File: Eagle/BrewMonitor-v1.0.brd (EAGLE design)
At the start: 41.6 x 50.2 mm, 18 parts, among them U1 ATMEGA328P_PDIP

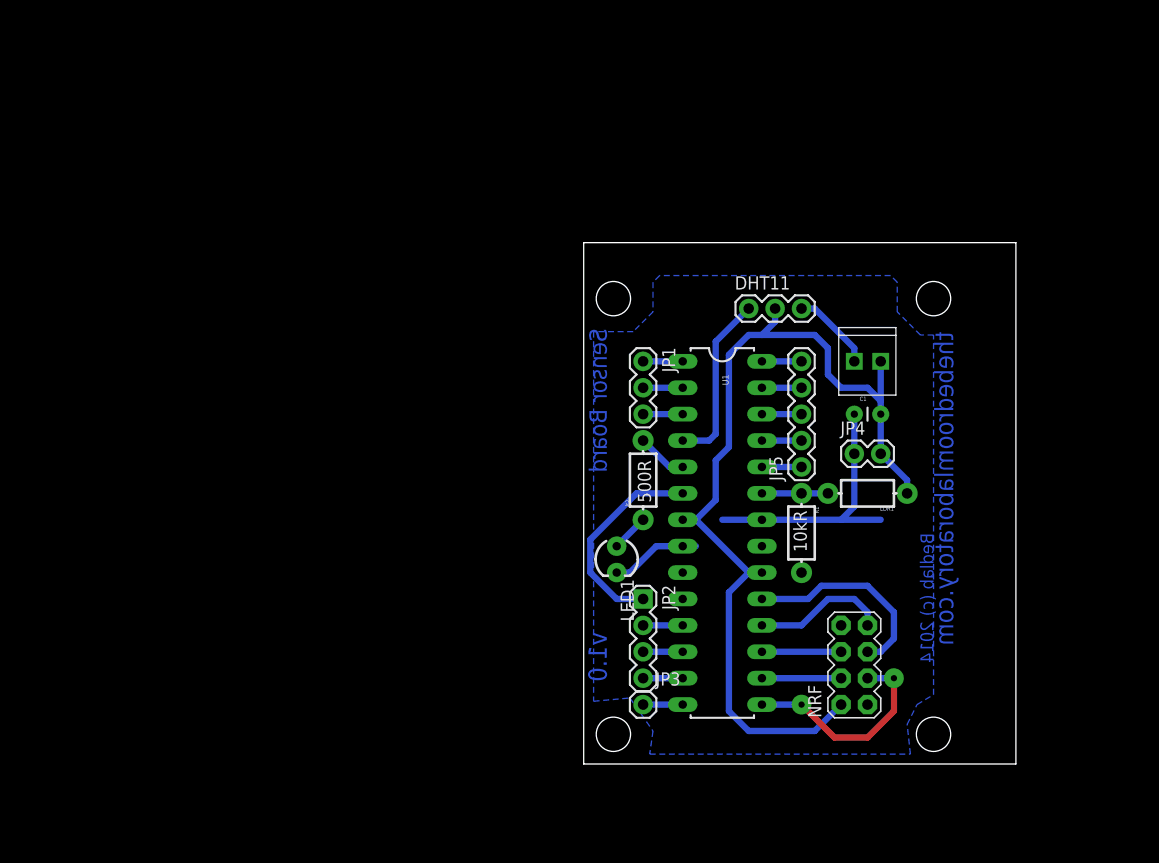
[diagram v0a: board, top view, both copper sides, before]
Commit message: Updated Eagle Schematic for the correct parts and made net connections. The brd file still needs updating.
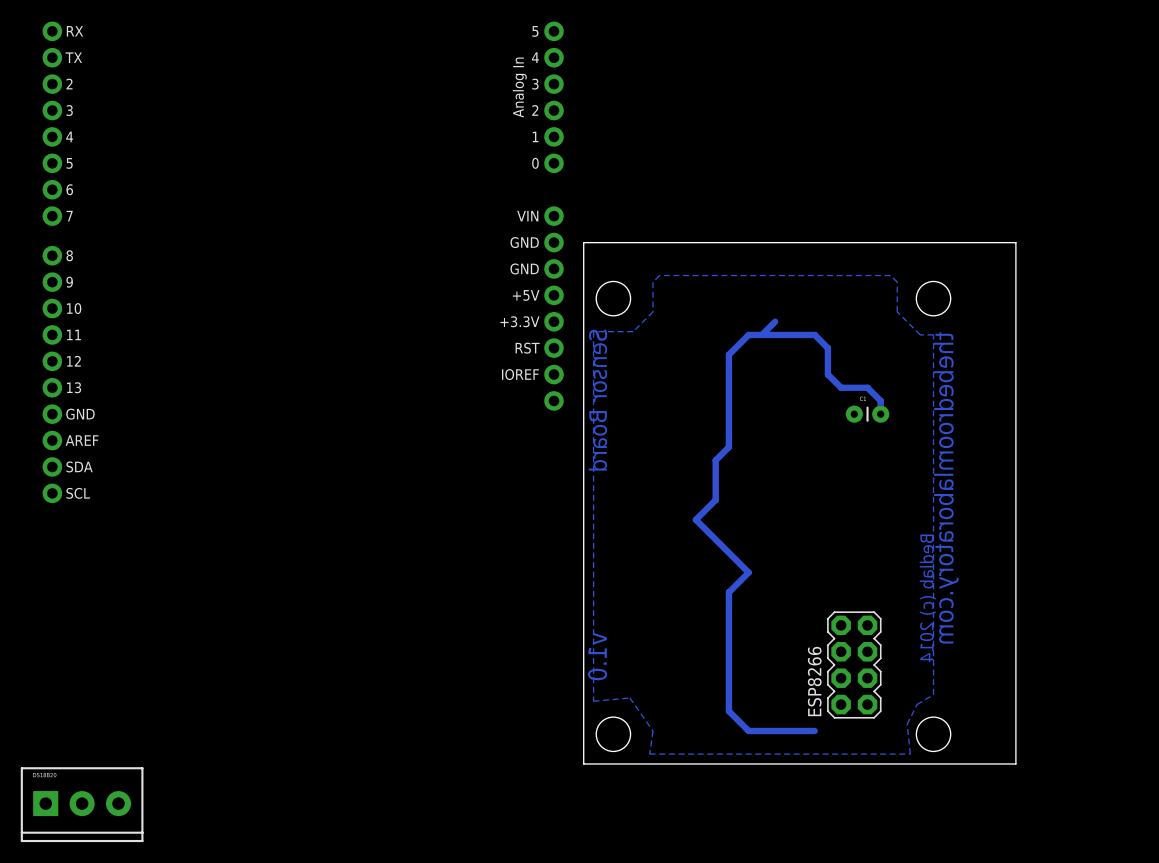
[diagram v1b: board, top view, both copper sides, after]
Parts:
- removed DHT11, JP1: (no value), SparkFun-Connectors:1X03
- removed JP2: (no value), SparkFun-Connectors:1X04
- removed JP3: M01PTH, SparkFun-Connectors:1X01
- removed JP4: M02PTH, SparkFun-Connectors:1X02
- removed JP5: (no value), SparkFun-Connectors:1X05
- removed LDR1: (no value), SparkFun-Passives:AXIAL-0.3-KIT
- removed LED1: (no value), SparkFun-LED:LED3MM
- removed POWER: M022.54MM_SCREWTERM, SparkFun-Connectors:1X02_2.54_SCREWTERM
- removed R1: 10kR, SparkFun-Passives:AXIAL-0.3-KIT
- removed R2: 500R, SparkFun-Passives:AXIAL-0.3-KIT
- removed U1: ATMEGA328P_PDIP, SparkFun-DigitalIC:DIL28-3
- added DS18B20: (no value), SparkFun-Connectors:SCREWTERMINAL-3.5MM-3
- added U$5: ARDUINO_R3_SHIELD, SparkFun-Boards:UNO_R3_SHIELD
- renumbered NRF to ESP8266
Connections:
- removed net A1: JP5.1, U1.24
- removed net A2: JP5.2, U1.25
- removed net A3: JP5.3, U1.26
- removed net A5: JP5.5, U1.28
- removed net D4: JP2.1, U1.6
- removed net D5: JP2.2, U1.11
- removed net D6: JP2.3, U1.12
- removed net D7: JP2.4, U1.13
- removed net D8: JP3.1, U1.14
- removed net N$1: LDR1.P$2, R1.P$1, U1.23
- removed net N$10: ESP8266.6, U1.17
- removed net N$2: LED1.A, R2.P$1
- removed net N$3: DHT11.1, U1.4
- removed net N$4: R2.P$2, U1.5
- removed net N$5: ESP8266.3, U1.15
- removed net N$6: ESP8266.4, U1.16
- removed net N$7: ESP8266.5, U1.19
- removed net N$9: ESP8266.7, U1.18
- removed net RESET: JP1.1, U1.1
- removed net VCC: C1.2, DHT11.2, ESP8266.2, JP4.2, LDR1.P$1, POWER.P1, U1.20, U1.7
- new net 3.3V: C1.2, ESP8266.7, U$5.3.3V
- new net 5V: DS18B20.1, U$5.5V
- new net N$11: ESP8266.3
- new net N$12: ESP8266.5
- new net N$15: ESP8266.4
- new net N$16: ESP8266.6
- net A4: now also DS18B20.3, U$5.A4; no longer JP5.4, U1.27
- net GND: now also DS18B20.2, ESP8266.2, U$5.GND@1, U$5.GND@2; no longer DHT11.3, ESP8266.1, JP4.1, LED1.K, POWER.P2, R1.P$2, U1.22, U1.8
- net RX: now also ESP8266.8, U$5.RX; no longer JP1.2, U1.2
- net TX: now also ESP8266.1, U$5.TX; no longer JP1.3, U1.3
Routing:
- net VCC: track 90.0 -> 0.00 mm
- net 3.3V: track 0.00 -> 70.1 mm
- net GND: track 42.5 -> 0.00 mm
- net N$5: track 20.8 -> 0.00 mm, vias 2 -> 0
- net D4: track 20.0 -> 0.00 mm
- net N$7: track 19.9 -> 0.00 mm
- net N$3: track 16.8 -> 0.00 mm
- net N$9: track 13.0 -> 0.00 mm
- net N$6: track 7.62 -> 0.00 mm
- net N$10: track 7.62 -> 0.00 mm
- net N$1: track 6.35 -> 0.00 mm
- net N$4: track 4.86 -> 0.00 mm
- net TX: track 3.81 -> 0.00 mm
- net RX: track 3.81 -> 0.00 mm
- net RESET: track 3.81 -> 0.00 mm
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
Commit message: Updated Schematic and Board files. Circuit now complete.
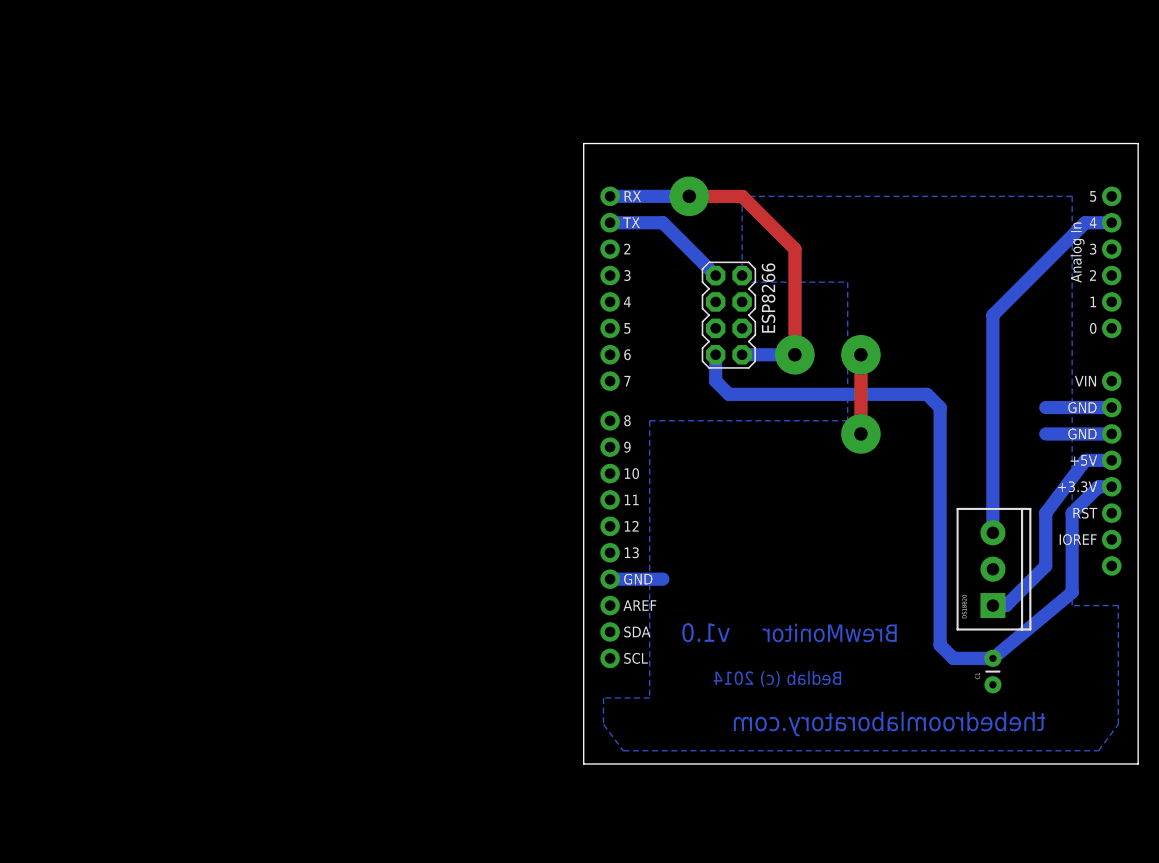
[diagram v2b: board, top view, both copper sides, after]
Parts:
- removed U$1, U$2, U$3, U$4: (no value), SparkFun-Electromechanical:STAND-OFF
- DS18B20: value (none) -> M03X1
- moved DS18B20 93.1 mm to (39.4, 15.2), turned to 90 degrees
- moved U$5 56.0 mm to (0.00, 0.00)
- moved ESP8266 35.8 mm to (14.0, 43.2), turned to 270 degrees
- moved C1 29.3 mm to (39.4, 7.62), turned to 90 degrees
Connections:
- removed net N$11: ESP8266.3
- removed net N$12: ESP8266.5
- removed net N$15: ESP8266.4
- removed net N$16: ESP8266.6
- net GND: now also U$5.GND@0
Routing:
- net A4: track 0.00 -> 36.1 mm
- net RX: track 0.00 -> 35.1 mm, vias 0 -> 2
- net GND: track 0.00 -> 25.4 mm, vias 0 -> 2
- net 5V: track 0.00 -> 20.6 mm
- net TX: track 0.00 -> 12.3 mm
- net 3.3V: track 70.1 -> 76.0 mm
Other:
- board size 41.6 x 50.2 mm -> 53.3 x 59.7 mm
- board text added: "BrewMonitor"
- board text removed: "Sensor Board"
